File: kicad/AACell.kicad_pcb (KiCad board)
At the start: 2 copper layers, 14.2 x 50.7 mm, 5 parts

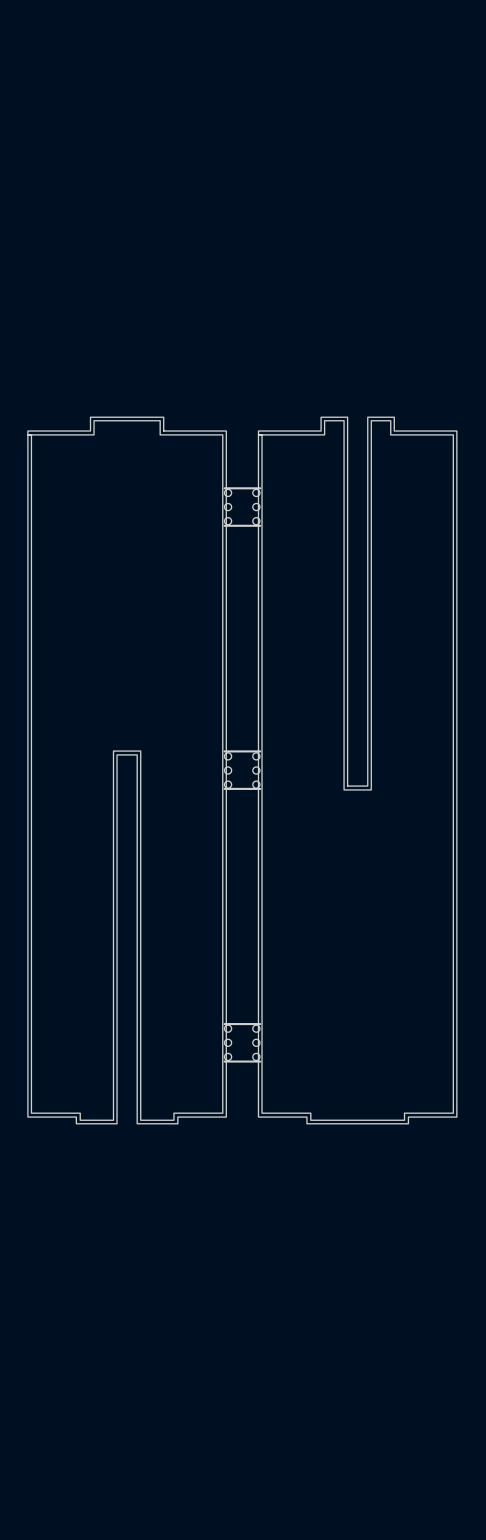
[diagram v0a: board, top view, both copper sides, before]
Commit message: Finished the inial circuit and layout.
Shortened on of the pieces to avoid the mechanical clash with the
Micro USB connector.
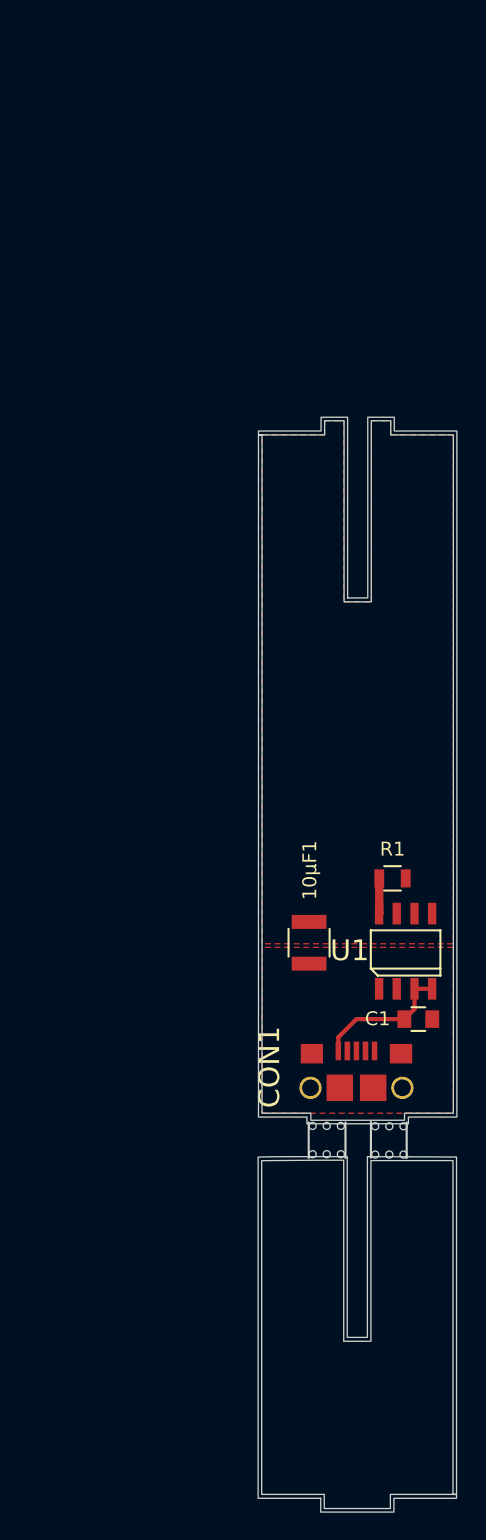
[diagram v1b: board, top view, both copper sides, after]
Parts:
- removed the REF** at (113.1, 52.7)
- added 10μF1: C, Capacitors_SMD:C_1210, F.Cu at (117.9, 84.0)
- added C1: 0.1μF, Capacitors_SMD:C_0805, F.Cu at (125.7, 89.5)
- added CON1: USB-MICRO-B, AACell-Footprint:USB_Micro_B, F.Cu at (121.3, 94.4)
- added R1: 250kΩ, Resistors_SMD:R_0805, F.Cu at (123.9, 79.4)
- added U1: TPS776xx, AACell-Footprint:SOIC_5.4_1.27, F.Cu at (124.8, 84.6)
- moved CB*** 43.8 mm to (121.3, 112.1), turned to 180 degrees
- moved REF** 28.6 mm to (123.6, 98.2), turned to 90 degrees
- moved REF** 9.25 mm to (119.1, 98.2), turned to 90 degrees
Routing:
- net Net-(C1-Pad1): track 0.00 -> 10.0 mm
- net /~RESET~/PG: track 0.00 -> 2.54 mm
- added copper zone on F.Cu, net /VOUT
- added copper zone on F.Cu, net GND
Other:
- outline, holes or cut-outs redrawn
- net class Default: clearance 0.2 -> 0.1524; trace_width 0.25 -> 0.1524; via_dia 0.6 -> 0.6858; via_drill 0.4 -> 0.3302
- rule pad_to_mask_clearance: 0.2 -> 0.0508
- rule trace_clearance: 0.2 -> 0.1524
- rule trace_min: 0.2 -> 0.1524
- rule via_min_drill: 0.3 -> 0.3302
- rule via_min_size: 0.4 -> 0.6858

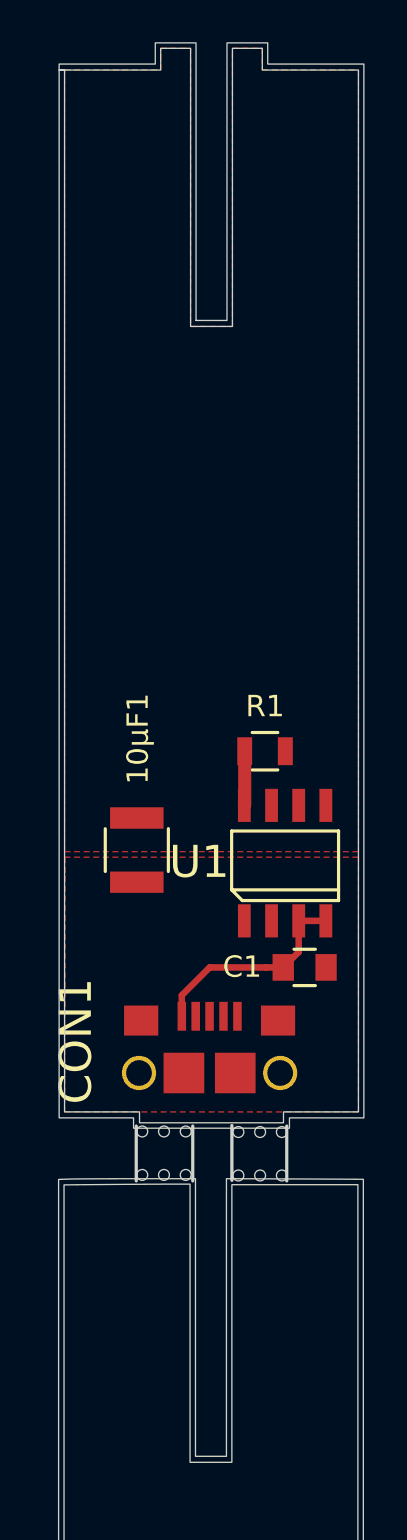
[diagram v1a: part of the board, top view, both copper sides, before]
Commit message: Added the SJM logo using the new technique for creating logos
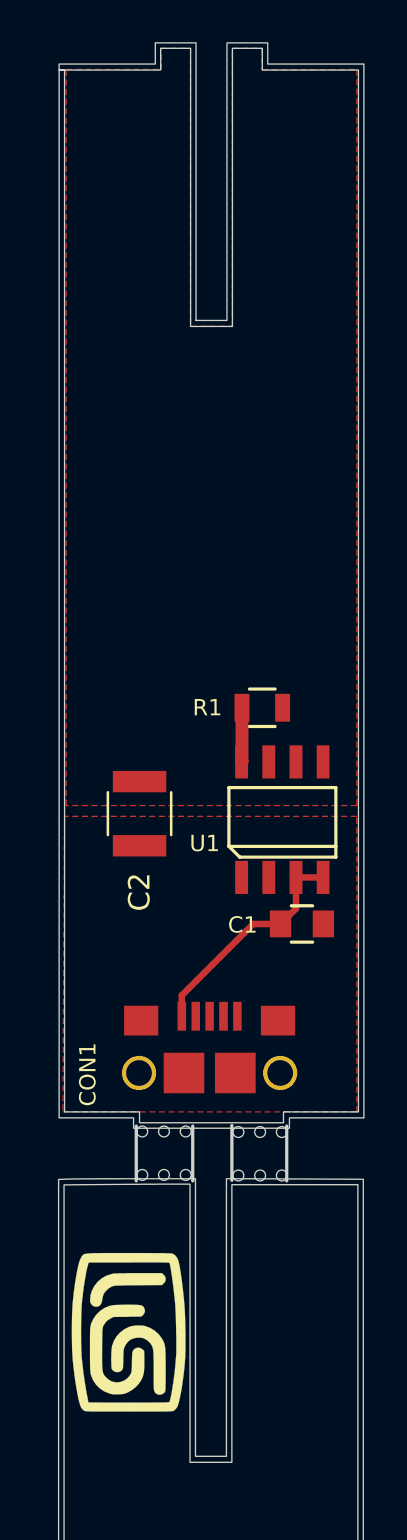
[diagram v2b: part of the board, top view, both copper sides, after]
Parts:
- removed 10μF1: C, Capacitors_SMD:C_1210
- added C2: 10μF, Capacitors_SMD:C_1210, F.Cu at (118.0, 82.3)
- added G***: LOGO, AACell-Footprint:SJM_7mm, F.Cu at (117.5, 106.6)
- moved C1 2.04 mm to (125.6, 87.5)
- moved R1 2.04 mm to (123.7, 77.3)
- moved U1 2.04 mm to (124.7, 82.6)
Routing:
- net Net-(C1-Pad1): track 10.0 -> 10.7 mm

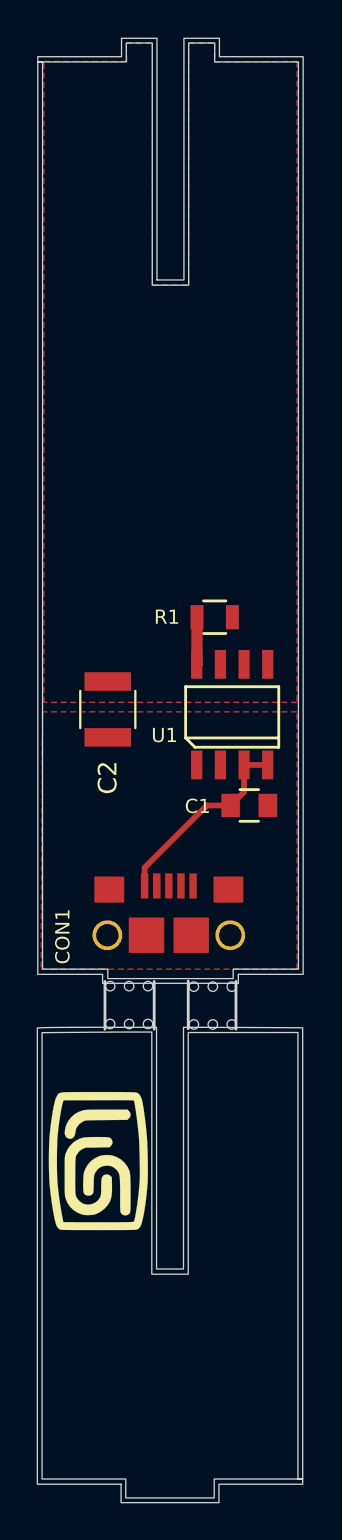
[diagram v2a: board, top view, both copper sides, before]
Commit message: Adds the PDF for the LDO and redesign of the edge cuts after the feedback from OSH Park
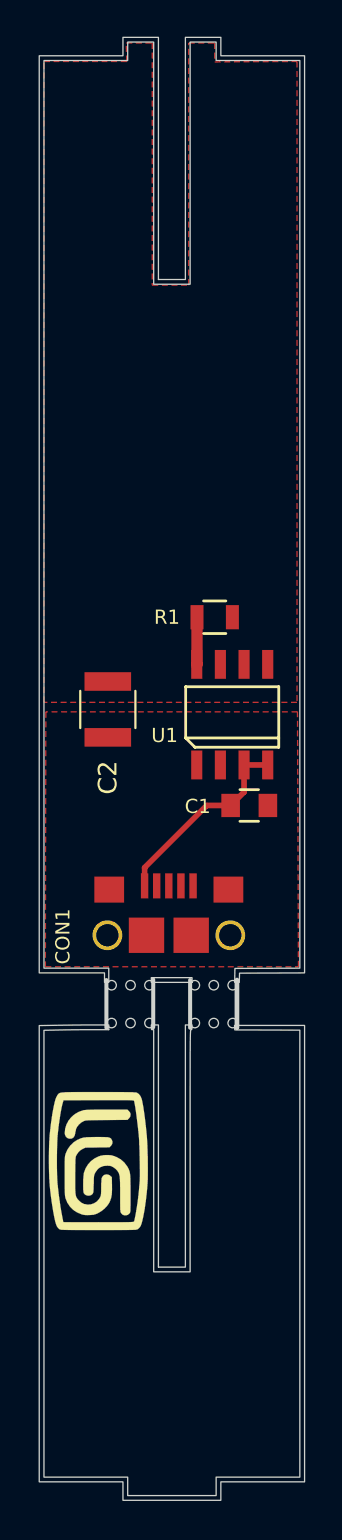
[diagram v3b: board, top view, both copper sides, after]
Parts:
- removed CB***: LOGO, AACell-Footprint:AACell-Slot-Bottom
- removed CT***: LOGO, AACell-Footprint:AACell-Slot-Top
- added B***: LOGO, AACell-Footprint:AACell-Both, F.Cu at (121.4, 85.5)
- moved REF** 0.09 mm to (123.7, 98.1)
- moved REF** 0.09 mm to (119.2, 98.1)
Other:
- board size 14.2 x 50.7 mm -> 14.2 x 78.6 mm
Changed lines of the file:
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@@
 (kicad_pcb (version 4) (host pcbnew 4.0.7)
   (general
-    (links 0)
-    (no_connects 2)
-    (area 117.755599 96.800599 124.941401 99.541401)
+    (links 15)
+    (no_connects 0)
+    (area 117.798849 96.691449 125.044201 99.517201)
     (thickness 1.6)
     (drawings 4)
     (tracks 8)
     (zones 0)
-    (modules 10)
+    (modules 9)
     (nets 5)
   )
@@
     (trace_min 0.1524)
     (segment_width 0.2)
-    (edge_width 0.15)
+    (edge_width 0.254)
     (via_size 0.6858)
     (via_drill 0.3302)
@@
   )
   (module AACell-Footprint:MouseBites (layer F.Cu)
-    (at 123.6218 98.1964 90)
+    (at 123.6726 98.1202 90)
     (fp_text reference REF** (at 0 1 180) (layer F.Fab) hide
       (effects (font (size 0.762 0.762) (thickness 0.127)))
@@
   )
   (module AACell-Footprint:MouseBites (layer F.Cu)
-    (at 119.126 98.171 90)
+    (at 119.2022 98.1202 90)
     (fp_text reference REF** (at 0 1 180) (layer F.Fab) hide
       (effects (font (size 0.762 0.762) (thickness 0.127)))
@@
     (pad 8 smd rect (at -1.905 -2.7) (size 0.6 1.55) (layers F.Cu F.Paste F.Mask)
       (net 4 /~RESET~/PG))
-  )
-  (module AACell-Footprint:AACell-Slot-Bottom (layer F.Cu)
-    (at 121.3358 112.141 180)
-    (fp_text reference CB*** (at 0 0 180) (layer F.SilkS) hide
-      (effects (font (size 0.762 0.762) (thickness 0.127)))
-    )
-    (fp_text value LOGO (at 0.75 0 180) (layer F.SilkS) hide
-      (effects (font (size 0.762 0.762) (thickness 0.127)))
-    )
-    (fp_poly (pts (xy 2.6416 -11.7602) (xy 7.1374 -11.7602) (xy 7.1374 12.742783) (xy 6.676128 12.759491)
-      (xy 6.58711 12.761781) (xy 6.451343 12.763978) (xy 6.272879 12.766061) (xy 6.055769 12.768009)
-      (xy 5.804065 12.769801) (xy 5.521817 12.771415) (xy 5.213078 12.772831) (xy 4.881898 12.774028)
-      (xy 4.532329 12.774984) (xy 4.168422 12.775678) (xy 3.794229 12.776089) (xy 3.475728 12.7762)
-      (xy 0.7366 12.7762) (xy 0.7366 -0.2032) (xy -0.7112 -0.2032) (xy -0.7112 12.7762)
-      (xy -2.67335 12.770097) (xy -3.026018 12.768956) (xy -3.394927 12.767682) (xy -3.772161 12.766308)
-      (xy -4.149803 12.764864) (xy -4.519939 12.763383) (xy -4.874652 12.761897) (xy -5.206026 12.760438)
-      (xy -5.506145 12.759038) (xy -5.767094 12.757729) (xy -5.87375 12.757155) (xy -7.112 12.750316)
-      (xy -7.112 -11.4808) (xy -6.858 -11.4808) (xy -6.858 12.4968) (xy -0.9652 12.4968)
-      (xy -0.9652 -0.4826) (xy 0.9906 -0.4826) (xy 0.9906 12.5222) (xy 2.05105 12.522181)
-      (xy 2.262017 12.521925) (xy 2.51625 12.521194) (xy 2.806217 12.52003) (xy 3.124387 12.518477)
-      (xy 3.463228 12.516578) (xy 3.815208 12.514376) (xy 4.172797 12.511914) (xy 4.528462 12.509235)
-      (xy 4.874672 12.506382) (xy 4.99745 12.505304) (xy 6.8834 12.488446) (xy 6.8834 -11.4808)
-      (xy 2.3876 -11.4808) (xy 2.3876 -12.4968) (xy -2.3622 -12.4968) (xy -2.3622 -11.4808)
-      (xy -6.858 -11.4808) (xy -7.112 -11.4808) (xy -7.112 -11.7602) (xy -2.6162 -11.7602)
-      (xy -2.6162 -12.7508) (xy 2.6416 -12.7508) (xy 2.6416 -11.7602)) (layer Edge.Cuts) (width 0.01))
-  )
-  (module AACell-Footprint:AACell-Slot-Top (layer F.Cu)
-    (at 121.3358 71.628)
-    (fp_text reference CT*** (at 0 0) (layer F.SilkS) hide
-      (effects (font (size 0.762 0.762) (thickness 0.127)))
-    )
-    (fp_text value LOGO (at 0.75 0) (layer F.SilkS) hide
-      (effects (font (size 0.762 0.762) (thickness 0.127)))
-    )
-    (fp_poly (pts (xy -0.7112 -12.3952) (xy 0.7366 -12.3952) (xy 0.7366 -25.3746) (xy 2.6416 -25.3746)
-      (xy 2.6416 -24.384) (xy 7.1374 -24.384) (xy 7.1374 24.892) (xy 3.6576 24.892)
-      (xy 3.6576 25.3746) (xy -3.6322 25.3746) (xy -3.6322 24.892) (xy -7.112 24.892)
-      (xy -7.112 -24.1046) (xy -6.858 -24.1046) (xy -6.858 24.6126) (xy -3.3528 24.6126)
-      (xy -3.3528 25.1206) (xy 3.3782 25.1206) (xy 3.3782 24.6126) (xy 6.8834 24.6126)
-      (xy 6.8834 -24.1046) (xy 2.3876 -24.1046) (xy 2.3876 -25.1206) (xy 0.9906 -25.1206)
-      (xy 0.9906 -12.1158) (xy -0.9652 -12.1158) (xy -0.9652 -25.1206) (xy -2.3622 -25.1206)
-      (xy -2.3622 -24.1046) (xy -6.858 -24.1046) (xy -7.112 -24.1046) (xy -7.112 -24.384)
-      (xy -2.6162 -24.384) (xy -2.6162 -25.3746) (xy -0.7112 -25.3746) (xy -0.7112 -12.3952)) (layer Edge.Cuts) (width 0.01))
   )
   (module Capacitors_SMD:C_1210 (layer F.Cu)
@@
       (xy -0.868176 -1.808294) (xy -0.799621 -1.808354) (xy -0.540711 -1.808454) (xy -0.327307 -1.808154)) (layer F.SilkS) (width 0.01))
   )
-  (gr_line (start 122.301 99.441) (end 122.301 96.8756) (layer Edge.Cuts) (width 0.15))
-  (gr_line (start 124.8664 99.4664) (end 124.8664 96.901) (layer Edge.Cuts) (width 0.15))
-  (gr_line (start 120.4722 99.4664) (end 120.4722 96.901) (layer Edge.Cuts) (width 0.15))
-  (gr_line (start 117.8306 99.4664) (end 117.8306 96.901) (layer Edge.Cuts) (width 0.15))
+  (module AACell-Footprint:AACell-Both (layer F.Cu)
+    (at 121.412 85.471)
+    (fp_text reference B*** (at 0 0) (layer F.SilkS) hide
+      (effects (font (thickness 0.3)))
+    )
+    (fp_text value LOGO (at 0.75 0) (layer F.SilkS) hide
+      (effects (font (thickness 0.3)))
+    )
+    (fp_poly (pts (xy -3.3782 14.0208) (xy -4.275754 14.0208) (xy -4.537135 14.021375) (xy -4.82874 14.023001)
+      (xy -5.134821 14.025524) (xy -5.439628 14.028792) (xy -5.727411 14.032654) (xy -5.982422 14.036958)
+      (xy -6.015654 14.037608) (xy -6.858001 14.054416) (xy -6.858001 26.051808) (xy -6.858 38.0492)
+      (xy -2.3622 38.0492) (xy -2.3622 39.0398) (xy 2.3876 39.0398) (xy 2.3876 38.0492)
+      (xy 6.8834 38.0492) (xy 6.8834 14.04655) (xy 3.3909 14.0335) (xy 3.375416 13.7922)
+      (xy 7.1374 13.7922) (xy 7.1374 38.3032) (xy 2.6416 38.3032) (xy 2.6416 39.2938)
+      (xy -2.6162 39.2938) (xy -2.6162 38.3032) (xy -7.112 38.3032) (xy -7.112 13.800464)
+      (xy -6.06425 13.783665) (xy -5.794307 13.779707) (xy -5.502523 13.776079) (xy -5.201455 13.772894)
+      (xy -4.903661 13.770266) (xy -4.621699 13.768308) (xy -4.368127 13.767133) (xy -4.19735 13.766833)
+      (xy -3.3782 13.7668) (xy -3.3782 14.0208)) (layer Edge.Cuts) (width 0.01))
+    (fp_poly (pts (xy -0.7112 26.7716) (xy 0.7366 26.7716) (xy 0.7366 13.7668) (xy 1.0922 13.7668)
+      (xy 1.0922 13.8938) (xy 1.089525 13.969975) (xy 1.078173 14.007966) (xy 1.053149 14.020256)
+      (xy 1.0414 14.0208) (xy 1.036096 14.021172) (xy 1.031176 14.02351) (xy 1.026623 14.029647)
+      (xy 1.022425 14.041416) (xy 1.018566 14.060651) (xy 1.015032 14.089184) (xy 1.011809 14.128848)
+      (xy 1.008883 14.181477) (xy 1.006239 14.248903) (xy 1.003864 14.33296) (xy 1.001742 14.435481)
+      (xy 0.999859 14.558298) (xy 0.998201 14.703245) (xy 0.996754 14.872155) (xy 0.995503 15.066861)
+      (xy 0.994435 15.289196) (xy 0.993534 15.540993) (xy 0.992786 15.824085) (xy 0.992178 16.140306)
+      (xy 0.991694 16.491487) (xy 0.991321 16.879463) (xy 0.991044 17.306067) (xy 0.990849 17.773131)
+      (xy 0.990722 18.282488) (xy 0.990647 18.835972) (xy 0.990611 19.435416) (xy 0.9906 20.082653)
+      (xy 0.9906 27.0256) (xy -0.9652 27.0256) (xy -0.9652 14.0208) (xy -1.0287 14.0208)
+      (xy -1.066387 14.016682) (xy -1.085188 13.995668) (xy -1.091599 13.944768) (xy -1.0922 13.8938)
+      (xy -1.0922 13.7668) (xy -0.7112 13.7668) (xy -0.7112 26.7716)) (layer Edge.Cuts) (width 0.01))
+    (fp_poly (pts (xy -0.7112 -26.2636) (xy 0.7366 -26.2636) (xy 0.7366 -39.2684) (xy 2.6416 -39.2684)
+      (xy 2.6416 -38.2778) (xy 7.1374 -38.2778) (xy 7.1374 10.972449) (xy 5.39115 10.978974)
+      (xy 3.6449 10.9855) (xy 3.63036 11.4808) (xy 3.384117 11.4808) (xy 3.396619 10.7315)
+      (xy 5.140009 10.724974) (xy 6.8834 10.718449) (xy 6.8834 -38.0238) (xy 2.3876 -38.0238)
+      (xy 2.3876 -39.0144) (xy 0.9906 -39.0144) (xy 0.9906 -26.0096) (xy -0.9652 -26.0096)
+      (xy -0.9652 -39.0144) (xy -2.3622 -39.0144) (xy -2.3622 -38.0238) (xy -6.858 -38.0238)
+      (xy -6.858 10.7188) (xy -3.3782 10.7188) (xy -3.3782 11.4808) (xy -3.6068 11.4808)
+      (xy -3.6068 10.9728) (xy -7.112 10.9728) (xy -7.112 -38.2778) (xy -2.6162 -38.2778)
+      (xy -2.6162 -39.2684) (xy -0.7112 -39.2684) (xy -0.7112 -26.2636)) (layer Edge.Cuts) (width 0.01))
+    (fp_poly (pts (xy 1.0922 11.4808) (xy -1.0922 11.4808) (xy -1.0922 11.2268) (xy 1.0922 11.2268)
+      (xy 1.0922 11.4808)) (layer Edge.Cuts) (width 0.01))
+  )
+  (gr_line (start 122.4026 99.3902) (end 122.4026 96.8248) (layer Edge.Cuts) (width 0.2159))
+  (gr_line (start 124.9172 99.3902) (end 124.9172 96.8248) (layer Edge.Cuts) (width 0.254))
+  (gr_line (start 120.4214 99.3648) (end 120.4214 96.7994) (layer Edge.Cuts) (width 0.2159))
+  (gr_line (start 117.9068 99.3902) (end 117.9068 96.8248) (layer Edge.Cuts) (width 0.2159))
   (segment (start 124.5776 87.4522) (end 123.2978 87.4522) (width 0.3048) (layer F.Cu) (net 3))
   (segment (start 123.2978 87.4522) (end 119.9596 90.7904) (width 0.3048) (layer F.Cu) (net 3))
@@
     (polygon
       (pts
-        (xy 114.4778 82.423) (xy 114.4016 96.2406) (xy 128.143 96.2406) (xy 128.143 82.423)
+        (xy 114.6556 82.423) (xy 114.6302 96.1136) (xy 128.2192 96.1136) (xy 128.1684 82.423)
       )
     )
